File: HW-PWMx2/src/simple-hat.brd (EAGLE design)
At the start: 87.3 x 61 mm, 36 parts, among them SW1 USER4

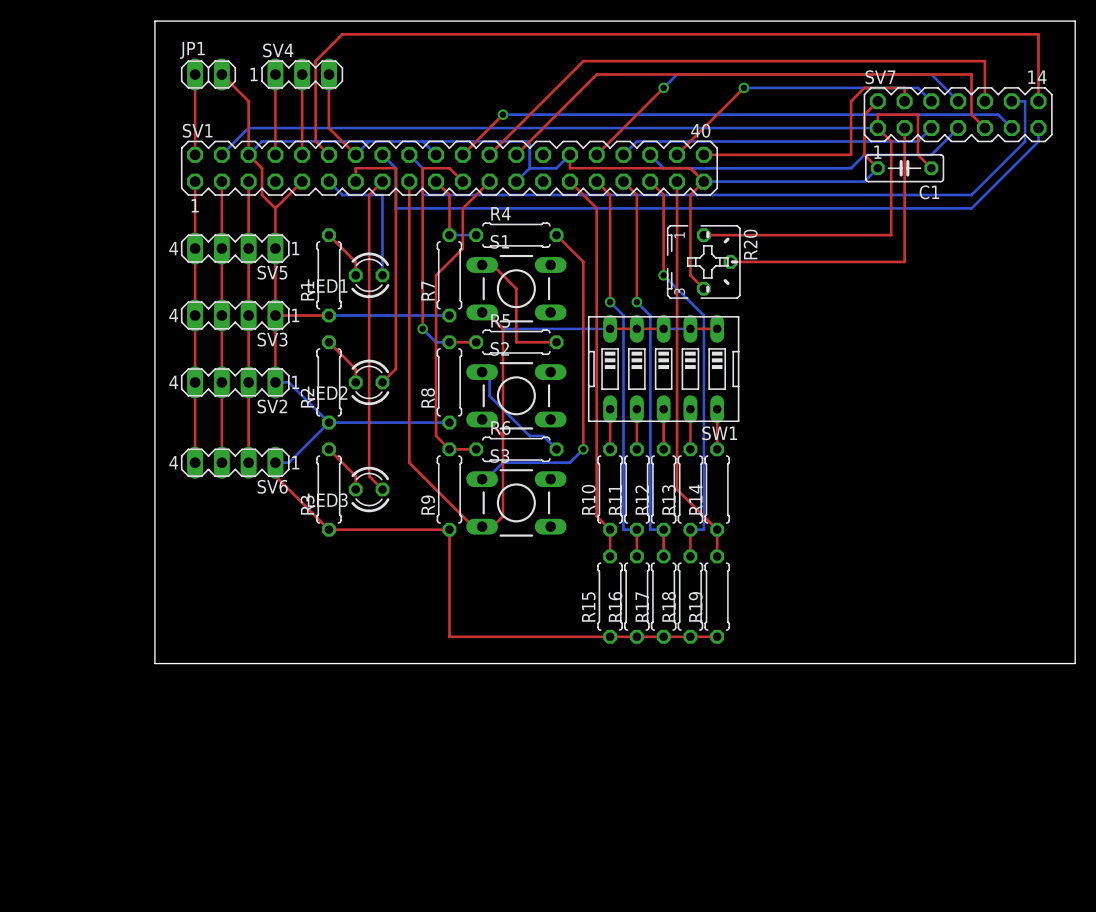
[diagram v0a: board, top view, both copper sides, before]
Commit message: Modified HW-PWMx2
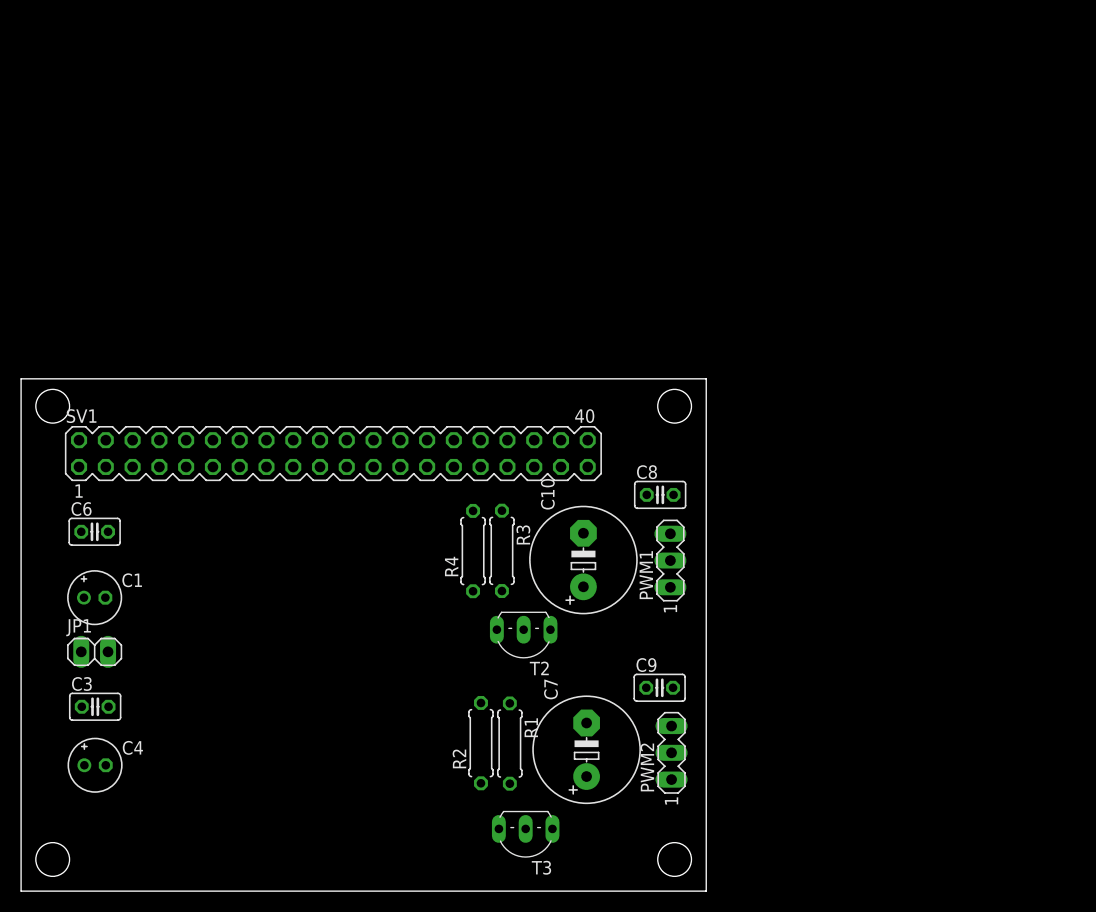
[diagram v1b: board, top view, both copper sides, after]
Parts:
- removed LED1: USER1, led:LED3MM
- removed LED2: USER2, led:LED3MM
- removed LED3: USER3, led:LED3MM
- removed R10, R11, R12, R13, R14, R5, R6: 1k, resistor:0207/7
- removed R15, R16, R17, R18, R19, R7, R8, R9: 10k, resistor:0207/7
- removed R20: 20k, pot:B25P
- removed S1, S2, S3: DTS-6, switch-tact:DTS-6
- removed SV2: I2C_1, con-lstb:MA04-1
- removed SV3: I2C_2, con-lstb:MA04-1
- removed SV4: UART, con-lstb:MA03-1
- removed SV5: I2C_3, con-lstb:MA04-1
- removed SV6: I2C_4, con-lstb:MA04-1
- removed SV7: LCD, con-lstb:MA07-2
- removed SW1: USER4, special:EDG-05
- added C10, C7: 1000uF, resistor:E5-10,5
- added C3, C6, C8, C9: 0.1uF, resistor:C025-025X050
- added C4: 10uF, resistor:E2-5
- added PWM1: JP2, con-lstb:MA03-1
- added PWM2: JP3, con-lstb:MA03-1
- added T2, T3: 2N2222, transistor:TO92-EBC
- C1: value 0.1 -> 10uF; device resistor:C050-025X075 -> resistor:E2-5
- R1, R3: value 270 -> 5.1k
- R2: value 270 -> 10k
- R4: value 1k -> 10k
- moved C1 87.0 mm to (6.98, 27.8), turned to 0 degrees
- moved JP1 55.8 mm to (6.98, 22.7)
- moved R1 47.6 mm to (46.4, 14.0), turned to 270 degrees
- moved R2 37.1 mm to (43.6, 14.0)
- moved R4 30.3 mm to (42.9, 32.3), turned to 90 degrees
- moved SV1 29.2 mm to (29.6, 41.5)
- moved R3 17.4 mm to (45.6, 32.3), turned to 270 degrees
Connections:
- removed net +3.3V_01: SV1.1, SV2.4, SV3.4, SV5.4, SV6.4
- removed net +3.3V_17: S1.3, S2.3, S3.3, SV1.17, SW1.1, SW1.2, SW1.3, SW1.4, SW1.5
- removed net +5V_04: C1.1, R20.A, SV1.4, SV7.1
- removed net DB0: SV1.36, SV7.7
- removed net DB1: SV1.32, SV7.8
- removed net DB2: SV1.26, SV7.9
- removed net DB3: SV1.24, SV7.10
- removed net DB4: SV1.22, SV7.11
- removed net DB5: SV1.18, SV7.12
- removed net DB6: SV1.16, SV7.13
- removed net DB7: SV1.12, SV7.14
- removed net E: SV1.38, SV7.6
- removed net GND34: SV1.34, SV7.5
- removed net GPIO10: R4.1, R7.2, SV1.19
- removed net GPIO11: R6.1, R9.2, SV1.23
- removed net GPIO13: R12.1, R17.2, SV1.33
- removed net GPIO17: LED1.A, SV1.11
- removed net GPIO19: R13.1, R18.2, SV1.35
- removed net GPIO22: LED3.A, SV1.15
- removed net GPIO26: R14.1, R19.2, SV1.37
- removed net GPIO27: LED2.A, SV1.13
- removed net GPIO5: R10.1, R15.2, SV1.29
- removed net GPIO6: R11.1, R16.2, SV1.31
- removed net GPIO9: R5.1, R8.2, SV1.21
- removed net I2C_SCL: SV1.5, SV2.2, SV3.2, SV5.2, SV6.2
- removed net I2C_SDA: SV1.3, SV2.3, SV3.3, SV5.3, SV6.3
- removed net N$1: LED1.K, R1.2
- removed net N$13: R11.2, SW1.7
- removed net N$14: R12.2, SW1.8
- removed net N$15: R10.2, SW1.6
- removed net N$18: R13.2, SW1.9
- removed net N$19: R14.2, SW1.10
- removed net N$8: R4.2, S3.1
- removed net RS: SV1.40, SV7.4
- removed net RXD0: SV1.10, SV4.2
- removed net TXD0: SV1.8, SV4.1
- removed net VO: R20.S, SV7.3
- new net N$4: R3.1, SV1.32
- new net N$6: R3.2, T2.B
- new net N$7: PWM1.1, R4.1, T2.C
- net +5V_02: now also C10.+, C3.1, C4.+, C7.+, C8.1, C9.1, PWM1.2, PWM2.2, R2.2, R4.2, SV1.4
- net GND: now also C1.-, C10.-, C3.2, C4.-, C6.2, C7.-, C8.2, C9.2, PWM1.3, PWM2.3, SV1.34, T2.E, T3.E; no longer C1.2, R1.1, R15.1, R16.1, R17.1, R18.1, R19.1, R2.1, R20.E, R3.1, R7.1, R8.1, R9.1, SV2.1, SV3.1, SV4.3, SV5.1, SV6.1, SV7.2
- net N$10: now also PWM2.1, R2.1, T3.C; no longer R6.2, S2.1
- net N$2: now also C1.+, C6.1, SV1.1; no longer LED2.K, R2.2
- net N$3: now also R1.1, SV1.33; no longer LED3.K, R3.2
- net N$9: now also R1.2, T3.B; no longer R5.2, S1.1
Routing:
- net GND: track 229.9 -> 0.00 mm
- net +5V_04: track 102.4 -> 0.00 mm
- net DB7: track 85.4 -> 0.00 mm
- net +3.3V_17: track 84.6 -> 0.00 mm
- net DB6: track 70.5 -> 0.00 mm
- net DB5: track 68.7 -> 0.00 mm
- net DB3: track 54.5 -> 0.00 mm
- net DB4: track 54.2 -> 0.00 mm, vias 1 -> 0
- net DB2: track 51.9 -> 0.00 mm
- net GPIO19: track 38.9 -> 0.00 mm, vias 1 -> 0
- net DB1: track 38.5 -> 0.00 mm, vias 1 -> 0
- net GPIO6: track 37.9 -> 0.00 mm, vias 1 -> 0
- net GPIO13: track 37.9 -> 0.00 mm, vias 1 -> 0
- net GPIO26: track 37.1 -> 0.00 mm
- net GPIO5: track 37.1 -> 0.00 mm
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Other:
- board size 87.3 x 61 mm -> 65 x 48.6 mm
